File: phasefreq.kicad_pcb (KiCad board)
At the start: 4 copper layers, 99 x 55.5 mm, 100 parts, among them J1 Power Input, J2 RF Input, J3 LO Input, J4 VCO Tune, U1 LM317_3PinPackage, U2 LM337_SOT223, U3 ADCMP564, U4 AD9901, U5 LM4040DIZ-2.5, U6 AD8676, U7 AD8676

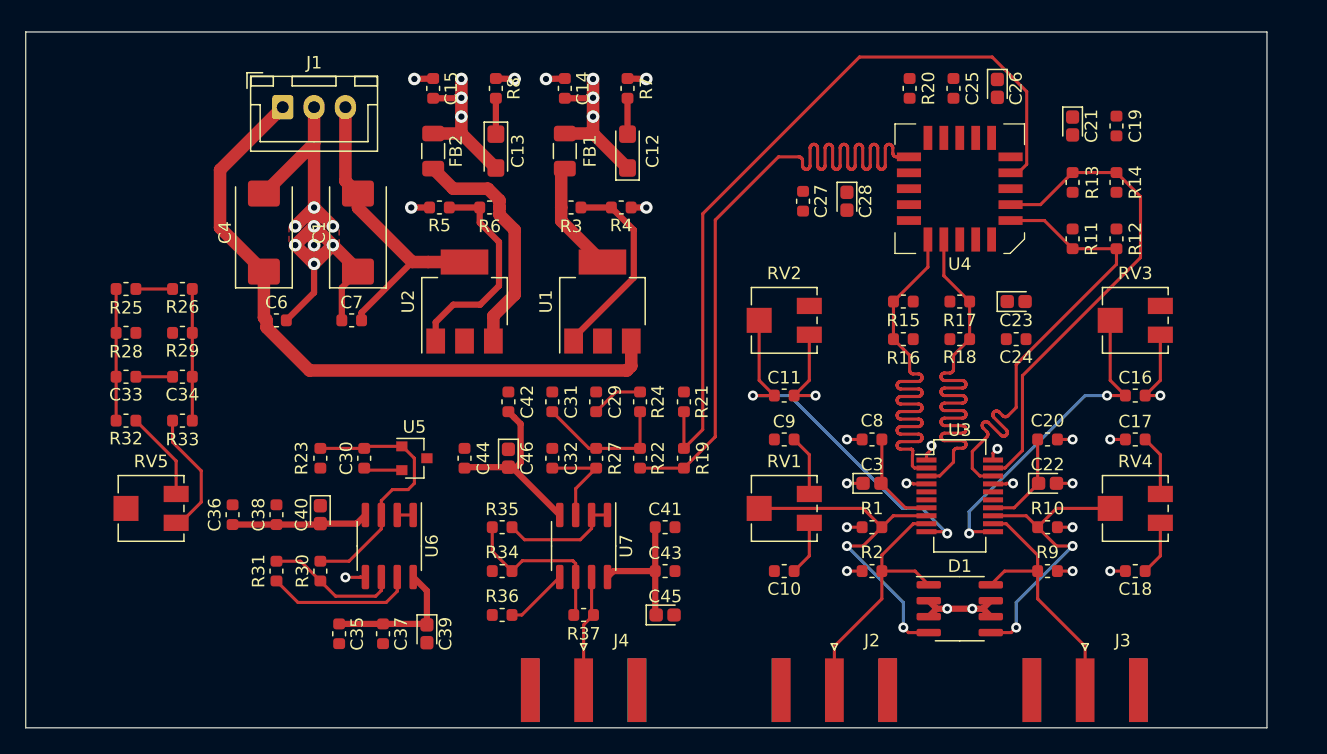
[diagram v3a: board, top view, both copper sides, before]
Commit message: routed almost everything, shrunk board dimensions a bit
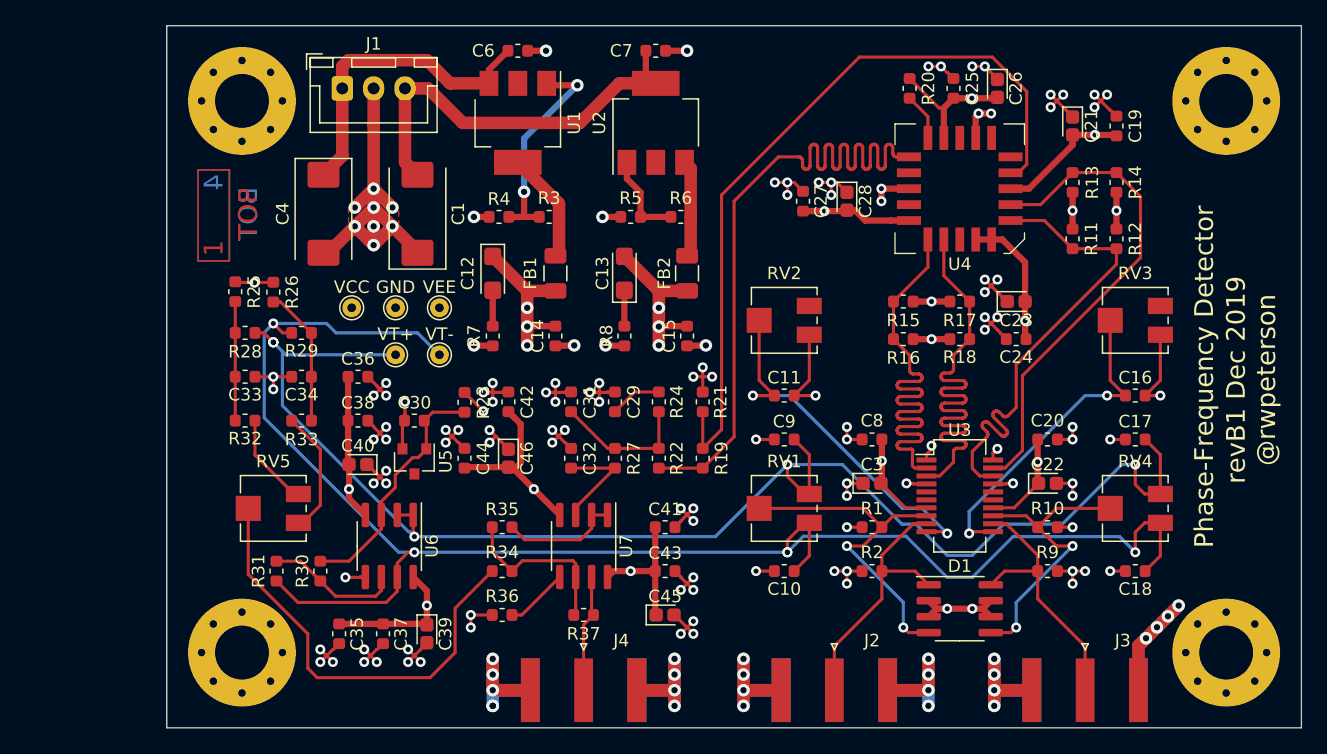
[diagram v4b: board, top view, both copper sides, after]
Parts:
- added GND: TestPoint_THTPad_D1.5mm_Drill0.7mm, TestPoint:TestPoint_THTPad_D1.5mm_Drill0.7mm, F.Cu at (140.5, 102.5)
- added REF**: MountingHole_4.3mm_M4_Pad_Via, MountingHole:MountingHole_4.3mm_M4_Pad_Via, F.Cu at (206.8, 130.0)
- added REF**: MountingHole_4.3mm_M4_Pad_Via, MountingHole:MountingHole_4.3mm_M4_Pad_Via, F.Cu at (206.8, 86.0)
- added REF**: MountingHole_4.3mm_M4_Pad_Via, MountingHole:MountingHole_4.3mm_M4_Pad_Via, F.Cu at (128.2, 86.0)
- added REF**: MountingHole_4.3mm_M4_Pad_Via, MountingHole:MountingHole_4.3mm_M4_Pad_Via, F.Cu at (128.2, 130.0)
- added VCC: TestPoint_THTPad_D1.5mm_Drill0.7mm, TestPoint:TestPoint_THTPad_D1.5mm_Drill0.7mm, F.Cu at (137.0, 102.5)
- added VEE: TestPoint_THTPad_D1.5mm_Drill0.7mm, TestPoint:TestPoint_THTPad_D1.5mm_Drill0.7mm, F.Cu at (144.0, 102.5)
- added VT+: TestPoint_THTPad_D1.5mm_Drill0.7mm, TestPoint:TestPoint_THTPad_D1.5mm_Drill0.7mm, F.Cu at (140.5, 106.2)
- added VT-: TestPoint_THTPad_D1.5mm_Drill0.7mm, TestPoint:TestPoint_THTPad_D1.5mm_Drill0.7mm, F.Cu at (144.0, 106.2)
- moved C7 32.4 mm to (161.2, 82.0), turned to 180 degrees
- moved C6 28.9 mm to (150.2, 82.0)
- moved C15 28.3 mm to (163.8, 104.8), turned to 90 degrees
- moved R7 22.5 mm to (148.2, 104.8), turned to 270 degrees
- moved FB2 22.5 mm to (163.8, 99.8), turned to 90 degrees
- moved R8 22.3 mm to (158.8, 104.8), turned to 90 degrees
- moved U2 20.9 mm to (161.2, 87.8)
- moved C14 19.8 mm to (153.2, 104.8), turned to 90 degrees
- moved U1 15.8 mm to (150.2, 87.8), turned to 270 degrees
- moved R5 15.3 mm to (159.2, 95.2)
- moved R6 15.3 mm to (163.2, 95.2)
- moved C36 14.9 mm to (137.5, 108.0), turned to 0 degrees
- moved C12 14.5 mm to (148.2, 99.8), turned to 270 degrees
- moved C13 14.1 mm to (158.8, 99.8), turned to 90 degrees
- moved R23 12.3 mm to (146.0, 110.0), turned to 90 degrees
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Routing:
- net VEE: track 46.4 -> 262.6 mm, vias 3 -> 12
- net GNDA: track 101.9 -> 285.5 mm, vias 33 -> 151
- net VTUNE-: track 20.6 -> 132.1 mm, vias 0 -> 5
- net VTUNE+: track 11.0 -> 116.9 mm, vias 0 -> 6
- net VCC: track 43.1 -> 146.0 mm, vias 3 -> 7
- net Net-(R34-Pad2): track 0.00 -> 35.3 mm
- net Net-(C4-Pad1): track 53.8 -> 25.2 mm
- net Net-(FB2-Pad2): track 18.8 -> 7.77 mm
- net Net-(R5-Pad1): track 17.1 -> 7.23 mm
- net Net-(C1-Pad2): track 25.1 -> 32.7 mm
- net Net-(R20-Pad1): track 0.00 -> 3.76 mm
- net Net-(C30-Pad2): track 21.4 -> 19.9 mm
- net Net-(R3-Pad2): track 15.8 -> 17.2 mm, vias 0 -> 2
- net Net-(C33-Pad2): track 10.5 -> 9.50 mm
- net ~PFD_OUT~: track 62.5 -> 61.9 mm
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- added copper zone on In2.Cu, net GNDA
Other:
- board size 99 x 55.5 mm -> 90.5 x 56 mm
- board text added: "1"
- board text added: "2"
- board text added: "3"
- board text added: "4"
- board text added: "BOT"
- board text added: "Phase-Frequency Detector"
- board text added: "TOP"
- board text added: "revB1 Dec 2019 @rwpeterson"
